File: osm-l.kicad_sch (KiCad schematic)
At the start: 19 parts, among them U14 OSM-L_Carrier-side

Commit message: [#82323] Update OSM connector pinout
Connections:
- net OSM_TEST_1V8: now reaches U14.AA33 (VCC_7_TEST)
- net ~{PWR_BTN}: now reaches U14.AA9 (~{PWR_BTN})
- net OSM_TEST_VDD_SOC: now reaches U14.B29 (VCC_8_TEST)
- net OSM_TEST_1V1: now reaches U14.C5 (VCC_6_TEST)
- net OSM_TEST_3V3: now reaches U14.M19 (VCC_2_TEST)
- net ~{BOOT_SEL1}: now reaches U14.R18 (~{BOOT_SEL1})
- net ~{RESET_IN}: now reaches U14.U17 (~{RESET_IN})
- net ~{BOOT_SEL0}: now reaches U14.U19 (~{BOOT_SEL0})
- net OSM_TEST_0V8: now reaches U14.Y16 (VCC_3_TEST)
- net OSM_TEST_1V0: now reaches U14.Y20 (VCC_4_TEST)
- net OSM_TEST_VDD_CPU: now reaches U14.Y3 (VCC_5_TEST)
- net ETH_VDDIO: no longer names the net of U14.M17 (ETH_IOPWR)
- no-connect marks 323 -> 328
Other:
- note added: "0.8V (LPDDR4)"
- note added: "0.92V (active) 0.65V (standby)"
- note added: "CPU_NVCC_BBSM"

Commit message: [#82323] Small OSM pinout fixes
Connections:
- net ~{PRSNT1}: no longer names the net of U14.G17 (GPIO_A_3)
- no-connect marks 328 -> 329
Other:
- moved on the sheet: U14H
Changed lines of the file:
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@@
 	)
 	(no_connect
-		(at 534.67 284.48)
+		(at 508 233.68)
 	)
 	(no_connect
@@
 	)
 	(no_connect
+		(at 96.52 134.62)
+	)
+	(no_connect
 		(at 142.24 234.95)
 	)
@@
 	)
 	(no_connect
-		(at 534.67 353.06)
+		(at 508 302.26)
 	)
 	(no_connect
@@
 	)
 	(no_connect
-		(at 534.67 304.8)
+		(at 508 254)
 	)
 	(no_connect
@@
 	)
 	(no_connect
-		(at 534.67 341.63)
+		(at 508 290.83)
 	)
 	(no_connect
@@
 	)
 	(no_connect
-		(at 534.67 339.09)
+		(at 508 288.29)
 	)
 	(no_connect
@@
 	)
 	(no_connect
-		(at 534.67 320.04)
+		(at 508 269.24)
 	)
 	(no_connect
@@
 	)
 	(no_connect
-		(at 534.67 293.37)
+		(at 508 242.57)
 	)
 	(no_connect
@@
 	)
 	(no_connect
-		(at 534.67 317.5)
+		(at 508 266.7)
 	)
 	(no_connect
@@
 	)
 	(no_connect
-		(at 534.67 361.95)
+		(at 508 311.15)
 	)
 	(no_connect
@@
 	)
 	(no_connect
-		(at 534.67 323.85)
+		(at 508 273.05)
 	)
 	(no_connect
@@
 	)
 	(no_connect
-		(at 534.67 297.18)
+		(at 508 246.38)
 	)
 	(no_connect
@@
 	)
 	(no_connect
-		(at 534.67 313.69)
+		(at 508 262.89)
 	)
 	(no_connect
@@
 	)
 	(no_connect
-		(at 534.67 326.39)
+		(at 508 275.59)
 	)
 	(no_connect
@@
 	)
 	(no_connect
-		(at 534.67 365.76)
+		(at 508 314.96)
 	)
 	(no_connect
@@
 	)
 	(no_connect
-		(at 534.67 355.6)
+		(at 508 304.8)
 	)
 	(no_connect
@@
 	)
 	(no_connect
-		(at 534.67 299.72)
+		(at 508 248.92)
 	)
 	(no_connect
@@
 	)
 	(no_connect
-		(at 534.67 368.3)
+		(at 508 317.5)
 	)
 	(no_connect
@@
 	)
 	(no_connect
-		(at 534.67 290.83)
+		(at 508 240.03)
 	)
 	(no_connect
@@
 	)
 	(no_connect
-		(at 534.67 307.34)
+		(at 508 256.54)
 	)
 	(no_connect
@@
 	)
 	(no_connect
-		(at 534.67 332.74)
+		(at 508 281.94)
 	)
 	(no_connect
@@
 	)
 	(no_connect
-		(at 534.67 359.41)
+		(at 508 308.61)
 	)
 	(no_connect
@@
 	)
 	(no_connect
-		(at 534.67 335.28)
+		(at 508 284.48)
 	)
 	(no_connect
@@
 	)
 	(no_connect
-		(at 534.67 346.71)
+		(at 508 295.91)
 	)
 	(no_connect
@@
 	)
 	(no_connect
-		(at 534.67 311.15)
+		(at 508 260.35)
 	)
 	(no_connect
@@
 	)
 	(no_connect
-		(at 534.67 349.25)
+		(at 508 298.45)
 	)
 	(no_connect
@@
 		)
 	)
-	(wire
-		(pts
-			(xy 73.66 237.49) (xy 96.52 237.49)
-		)
-		(stroke
-			(width 0)
-			(type default)
-		)
-	)
 	(bus
 		(pts
@@
 	(wire
 		(pts
-			(xy 73.66 255.27) (xy 68.58 255.27)
+			(xy 80.01 237.49) (xy 96.52 237.49)
 		)
 		(stroke
@@
 	(wire
 		(pts
-			(xy 73.66 255.27) (xy 73.66 237.49)
-		)
-		(stroke
-			(width 0)
-			(type default)
-		)
-	)
-	(wire
-		(pts
 			(xy 412.75 316.23) (xy 426.72 316.23)
 		)
@@
 		)
 	)
-	(wire
-		(pts
-			(xy 68.58 134.62) (xy 96.52 134.62)
-		)
-		(stroke
-			(width 0)
-			(type default)
-		)
-	)
 	(bus
 		(pts
@@
 	(hierarchical_label "DISP_BL_PWM"
 		(shape bidirectional)
-		(at 68.58 255.27 180)
+		(at 80.01 237.49 180)
 		(effects
 			(font
@@
 		)
 	)
-	(hierarchical_label "~{PRSNT1}"
-		(shape bidirectional)
-		(at 68.58 134.62 180)
-		(effects
-			(font
-				(size 1.27 1.27)
-			)
-			(justify right)
-		)
-	)
 	(hierarchical_label "OSM_ETH_C{SGMII}"
 		(shape bidirectional)
@@
 		)
 	)
-	(hierarchical_label "LVDS_TO_DP_EN"
-		(shape output)
-		(at 58.42 119.38 180)
-		(effects
-			(font
-				(size 1.27 1.27)
-			)
-			(justify right)
-		)
-	)
 	(hierarchical_label "I2C_I3C_1V8_15{I3C}"
 		(shape bidirectional)
@@
 	(symbol
 		(lib_id "antmicroModules:OSM-L_Carrier-side")
-		(at 534.67 284.48 0)
+		(at 508 233.68 0)
 		(unit 8)
 		(exclude_from_sim no)
@@
 		(fields_autoplaced yes)
 		(property "Reference" "U14"
-			(at 576.58 326.39 0)
+			(at 549.91 275.59 0)
 			(effects
 				(font
@@
 		)
 		(property "Value" "OSM-L_Carrier-side"
-			(at 594.36 292.1 0)
+			(at 567.69 241.3 0)
 			(effects
 				(font
@@
 		)
 		(property "Footprint" "antmicro-footprints:OSM-L_Carrier-side"
-			(at 594.36 294.64 0)
+			(at 567.69 243.84 0)
 			(effects
 				(font
@@
 		)
 		(property "Datasheet" "https://sget.org/standards/osm/"
-			(at 594.36 297.18 0)
+			(at 567.69 246.38 0)
 			(effects
 				(font
@@
 		)
 		(property "Description" "Open Standard Module (OSM)"
-			(at 618.49 299.72 0)
+			(at 591.82 248.92 0)
 			(effects
 				(font
@@
 		)
 		(property "MPN" ""
-			(at 618.49 289.56 0)
+			(at 591.82 238.76 0)
 			(effects
 				(font
@@
 		)
 		(property "Manufacturer" ""
-			(at 618.49 302.26 0)
+			(at 591.82 251.46 0)
 			(effects
 				(font
@@
 		)
 		(property "Author" "Antmicro"
-			(at 594.36 304.8 0)
+			(at 567.69 254 0)
 			(effects
 				(font
@@
 		)
 		(property "License" "Apache-2.0"
-			(at 594.36 307.34 0)
+			(at 567.69 256.54 0)
 			(effects
 				(font

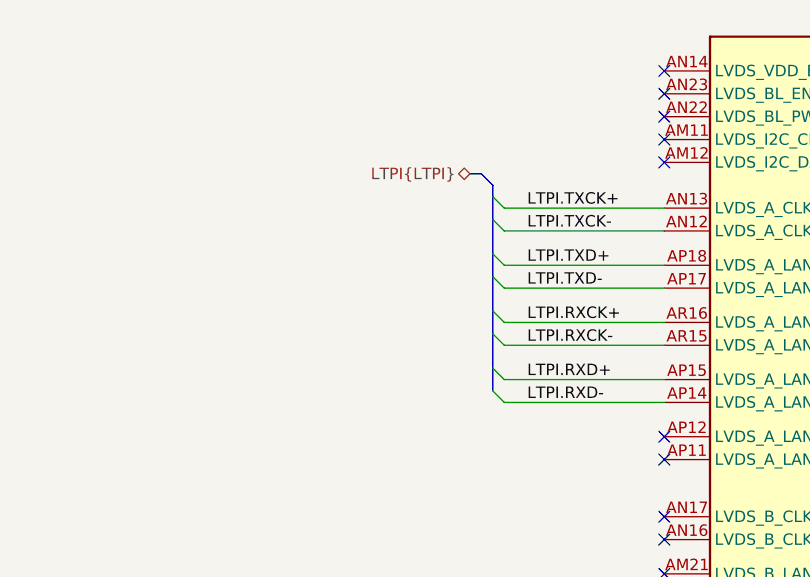
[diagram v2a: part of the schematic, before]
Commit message: [#83362] Fix connections of headers, add I2C mux
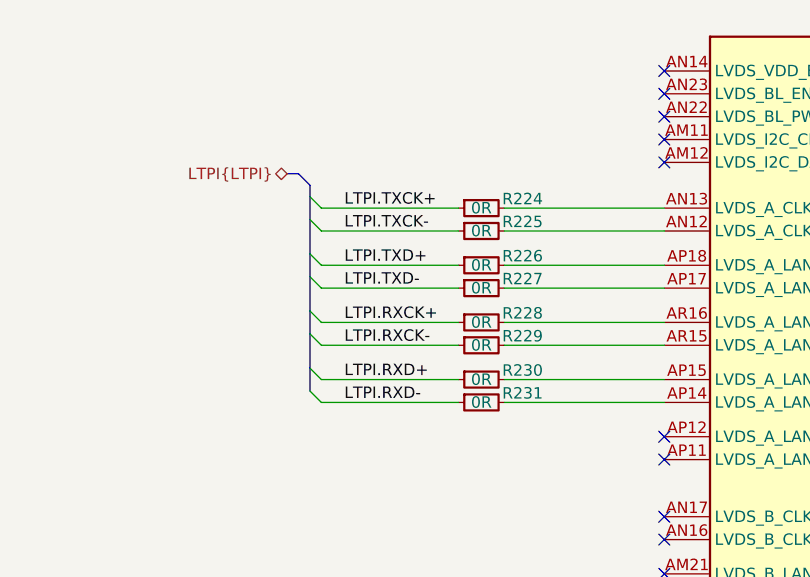
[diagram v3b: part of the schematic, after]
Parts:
- added R224, R225, R226, R227, R228, R229, R230, R231: R_0R_0402, antmicro-footprints:R_0402_1005Metric, symbol antmicroResistors0402:R_0R_0402
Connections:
- net LTPI.RXCK+: now also R228.1; no longer U14.AR16 (LVDS_A_LANE1_P)
- net LTPI.RXCK-: now also R229.1; no longer U14.AR15 (LVDS_A_LANE1_N)
- net LTPI.RXD+: now also R230.1; no longer U14.AP15 (LVDS_A_LANE2_P)
- net LTPI.RXD-: now also R231.1; no longer U14.AP14 (LVDS_A_LANE2_N)
- net LTPI.TXCK+: now also R224.1; no longer U14.AN13 (LVDS_A_CLK_P)
- net LTPI.TXCK-: now also R225.1; no longer U14.AN12 (LVDS_A_CLK_N)
- net LTPI.TXD+: now also R226.1; no longer U14.AP18 (LVDS_A_LANE0_P)
- net LTPI.TXD-: now also R227.1; no longer U14.AP17 (LVDS_A_LANE0_N)
- new net: R225.2, U14.AN12 (LVDS_A_CLK_N)
- new net: R224.2, U14.AN13 (LVDS_A_CLK_P)
- new net: R227.2, U14.AP17 (LVDS_A_LANE0_N)
- new net: R229.2, U14.AR15 (LVDS_A_LANE1_N)
- new net: R226.2, U14.AP18 (LVDS_A_LANE0_P)
- new net: R231.2, U14.AP14 (LVDS_A_LANE2_N)
- new net: R230.2, U14.AP15 (LVDS_A_LANE2_P)
- new net: R228.2, U14.AR16 (LVDS_A_LANE1_P)

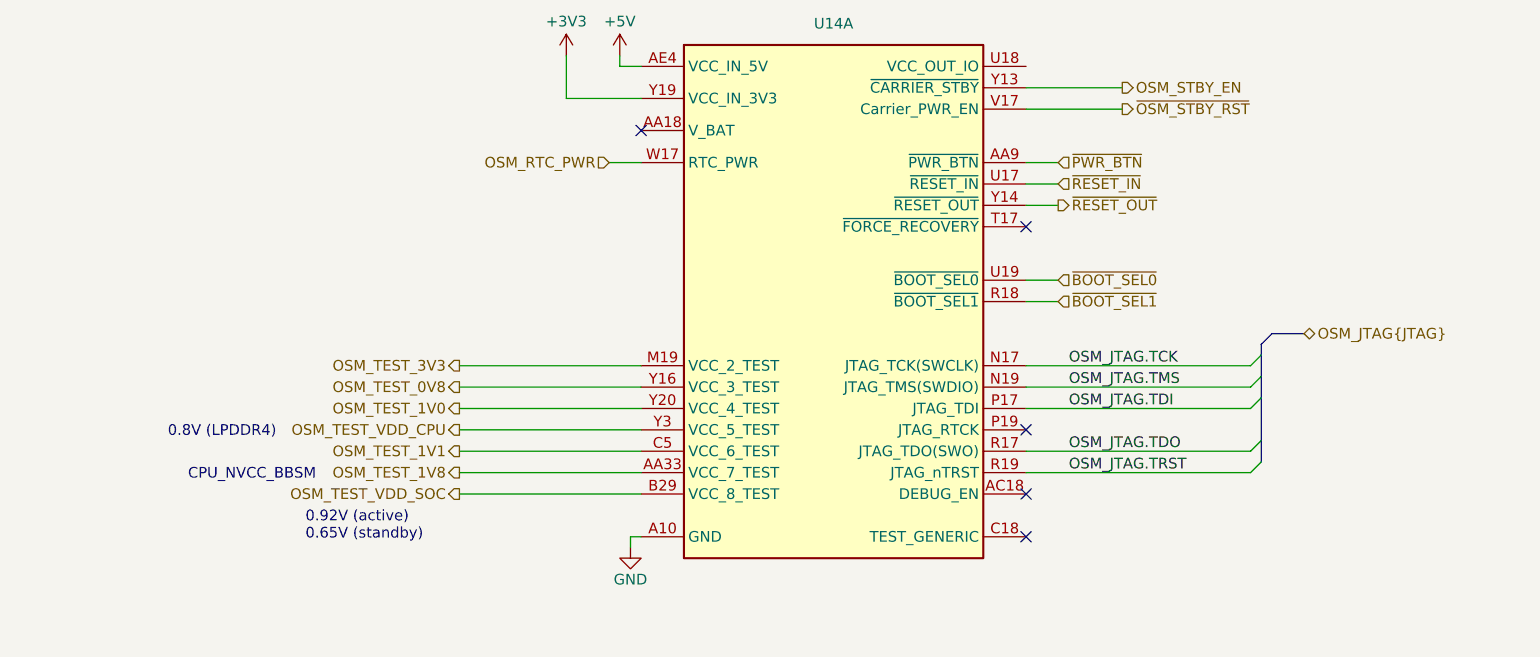
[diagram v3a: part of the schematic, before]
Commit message: [#83609] Add power pushbutton
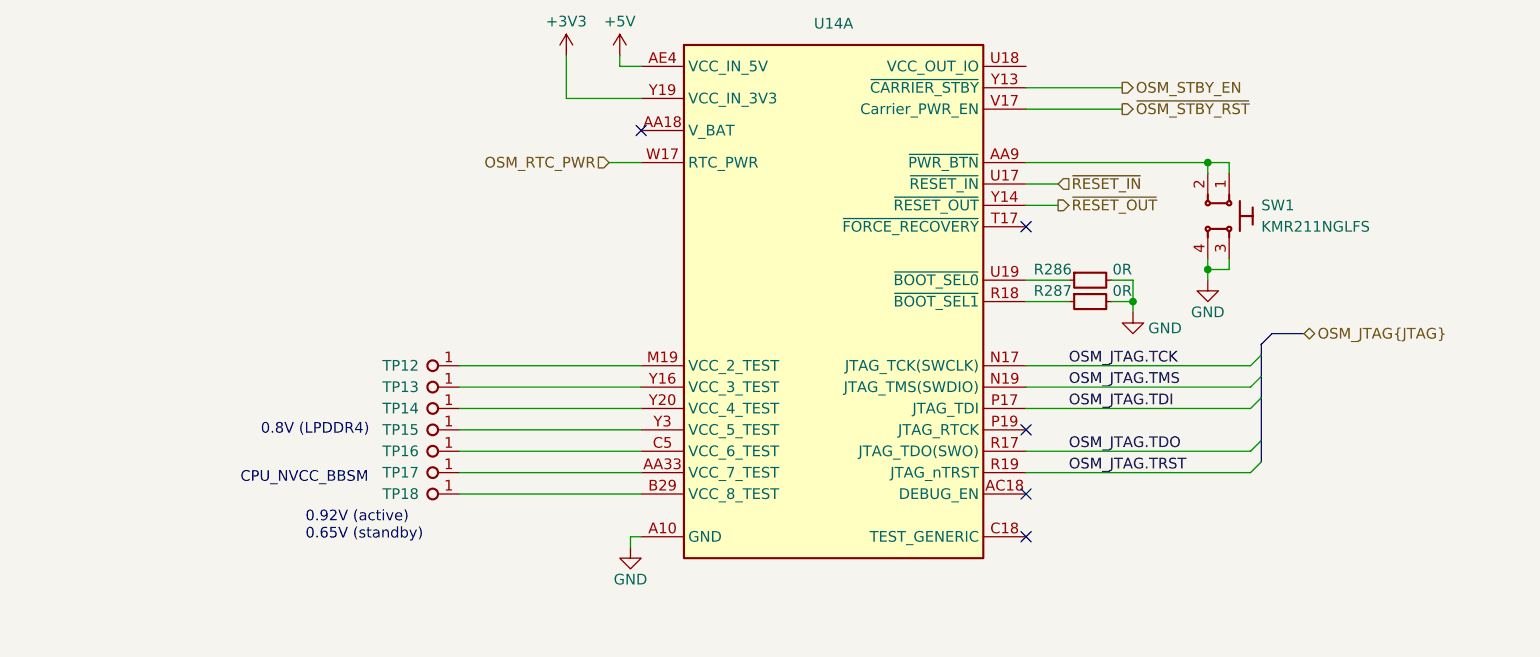
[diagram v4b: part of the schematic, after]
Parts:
- added R286, R287: R_0R_0402, antmicro-footprints:R_0402_1005Metric, symbol antmicroResistors0402:R_0R_0402
- added SW1: SW_KMR211NGLFS_SMD, antmicro-footprints:SW_KMR211NGLFS_SMD, symbol antmicroPushbuttonSwitches:SW_KMR211NGLFS_SMD
- added TP12, TP13, TP14, TP15, TP16, TP17, TP18: TP_0.75mm_SMD, antmicro-footprints:TP_SMD_0.75mm, symbol antmicroTestPoints:TP_0.75mm_SMD
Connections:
- net GND: now also R286.2, R287.2, SW1.3, SW1.4
- net OSM_TEST_0V8: no longer names the net of U14.Y16 (VCC_3_TEST)
- net OSM_TEST_0V8: now also TP13.1
- net OSM_TEST_1V0: no longer names the net of U14.Y20 (VCC_4_TEST)
- net OSM_TEST_1V0: now also TP14.1
- net OSM_TEST_1V1: no longer names the net of U14.C5 (VCC_6_TEST)
- net OSM_TEST_1V1: now also TP16.1
- net OSM_TEST_1V8: no longer names the net of U14.AA33 (VCC_7_TEST)
- net OSM_TEST_1V8: now also TP17.1
- net OSM_TEST_3V3: no longer names the net of U14.M19 (VCC_2_TEST)
- net OSM_TEST_3V3: now also TP12.1
- net OSM_TEST_VDD_CPU: no longer names the net of U14.Y3 (VCC_5_TEST)
- net OSM_TEST_VDD_CPU: now also TP15.1
- net OSM_TEST_VDD_SOC: no longer names the net of U14.B29 (VCC_8_TEST)
- net OSM_TEST_VDD_SOC: now also TP18.1
- net ~{BOOT_SEL0}: no longer names the net of U14.U19 (~{BOOT_SEL0})
- net ~{BOOT_SEL0}: now also R286.1
- net ~{BOOT_SEL1}: no longer names the net of U14.R18 (~{BOOT_SEL1})
- net ~{BOOT_SEL1}: now also R287.1
- net ~{PWR_BTN}: no longer names the net of U14.AA9 (~{PWR_BTN})
- net ~{PWR_BTN}: now also SW1.1, SW1.2

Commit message: [#83609] Add power push button emulator
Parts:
- added C157, C158: C_100n_25V_0402, antmicro-footprints:C_0402_1005Metric, symbol antmicroCapacitors0402:C_100n_25V_0402
- added C159, C160: C_1u_0402, antmicro-footprints:C_0402_1005Metric, symbol antmicroCapacitors0402:C_1u_0402
- added D13: RB521S30T1G, antmicro-footprints:SOD-523, symbol antmicroDiodesRectifiersSingle:RB521S30T1G
- added R288: R_100k_0402, antmicro-footprints:R_0402_1005Metric, symbol antmicroResistors0402:R_100k_0402
- added R289, R290: R_10k_0402, antmicro-footprints:R_0402_1005Metric, symbol antmicroResistors0402:R_10k_0402
- added R291: R_220R_0402, antmicro-footprints:R_0402_1005Metric, symbol antmicroResistors0402:R_220R_0402
- added U39, U40: 74AUP2G132, antmicro-footprints:VSSOP-8_2.3x2mm_P0.5mm, symbol antmicroLogicGatesandInverters:74AUP2G132
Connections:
- net GND: now also C157.1, C158.1, C159.1, C160.1, U39.4 (GND), U40.4 (GND)
- net ~{PWR_BTN}: now reaches SW1.1, SW1.2, U14.AA9 (~{PWR_BTN})
- net ~{PWR_BTN}: now also D13.2 (A), R290.1
- net +3V3 renamed +3V3_AON
- net +3V3_AON: now also C157.2, C158.2, R288.2, R289.2, U39.8 (VCC), U40.8 (VCC)
- net +5V renamed +5V_AON
- new net: D13.1 (C), R291.2
- new net: C159.2, R289.1, U40.1 (1A), U40.2 (1B)
- new net: C160.2, R288.1, U40.5 (2A), U40.6 (2B)
- new net +1V8_AON: R290.2
- new net S1: U39.1 (1A), U39.2 (1B), U40.7 (1Y)
- new net S2: U39.5 (2A), U40.3 (2Y)
- new net ~{S1}: U39.6 (2B), U39.7 (1Y)
- new net ~~{S1}S2: R291.1, U39.3 (2Y)
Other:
- note added: "3V3_AON S1 S2 ~{S1} ~{S1}S2 ~~{S1}S2"
- note added: "Auto-startup pushbutton emulator"
- note added: "_/¯¯¯¯¯¯¯¯¯¯¯¯¯¯¯¯ _/¯¯¯¯\___________ _/¯¯¯¯¯¯¯\________ _/\___/¯¯¯¯¯¯¯¯¯¯¯ _/\___/¯¯\________ _//¯¯¯\__/¯¯¯¯¯¯¯¯"
- moved on the sheet: C134, C135, C136, C137, C138, C139, R185, R186, R187, R188, R189, R190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
